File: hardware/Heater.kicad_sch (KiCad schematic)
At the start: 16 parts

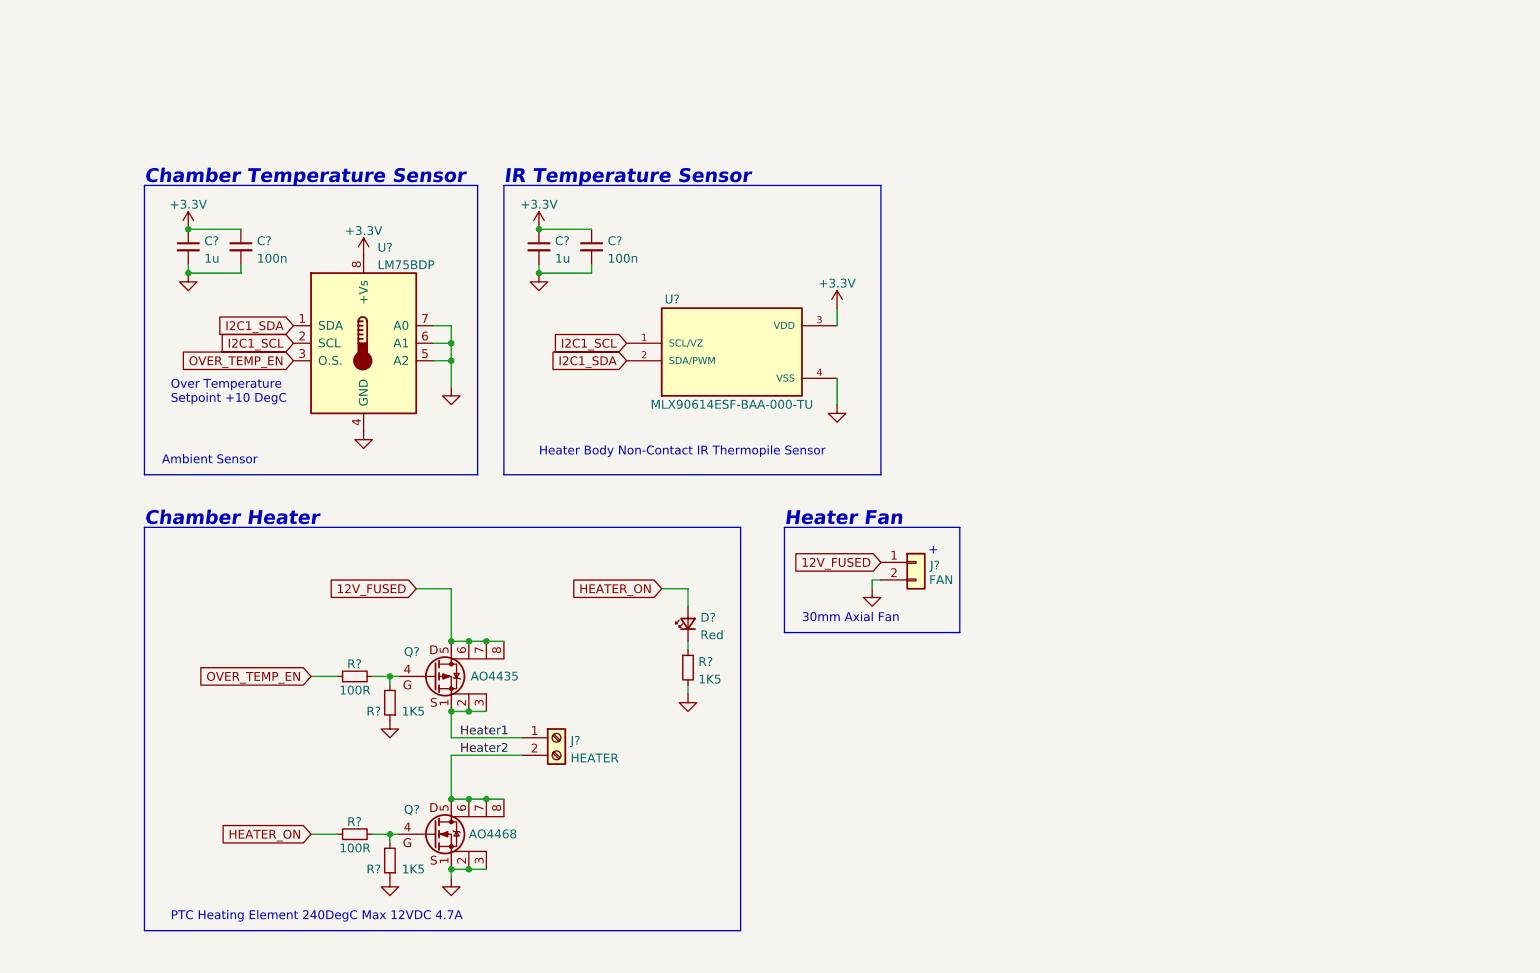
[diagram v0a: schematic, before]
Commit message: schematics finished, footprints assigned. Still need to fix foorptints for MOSFETS
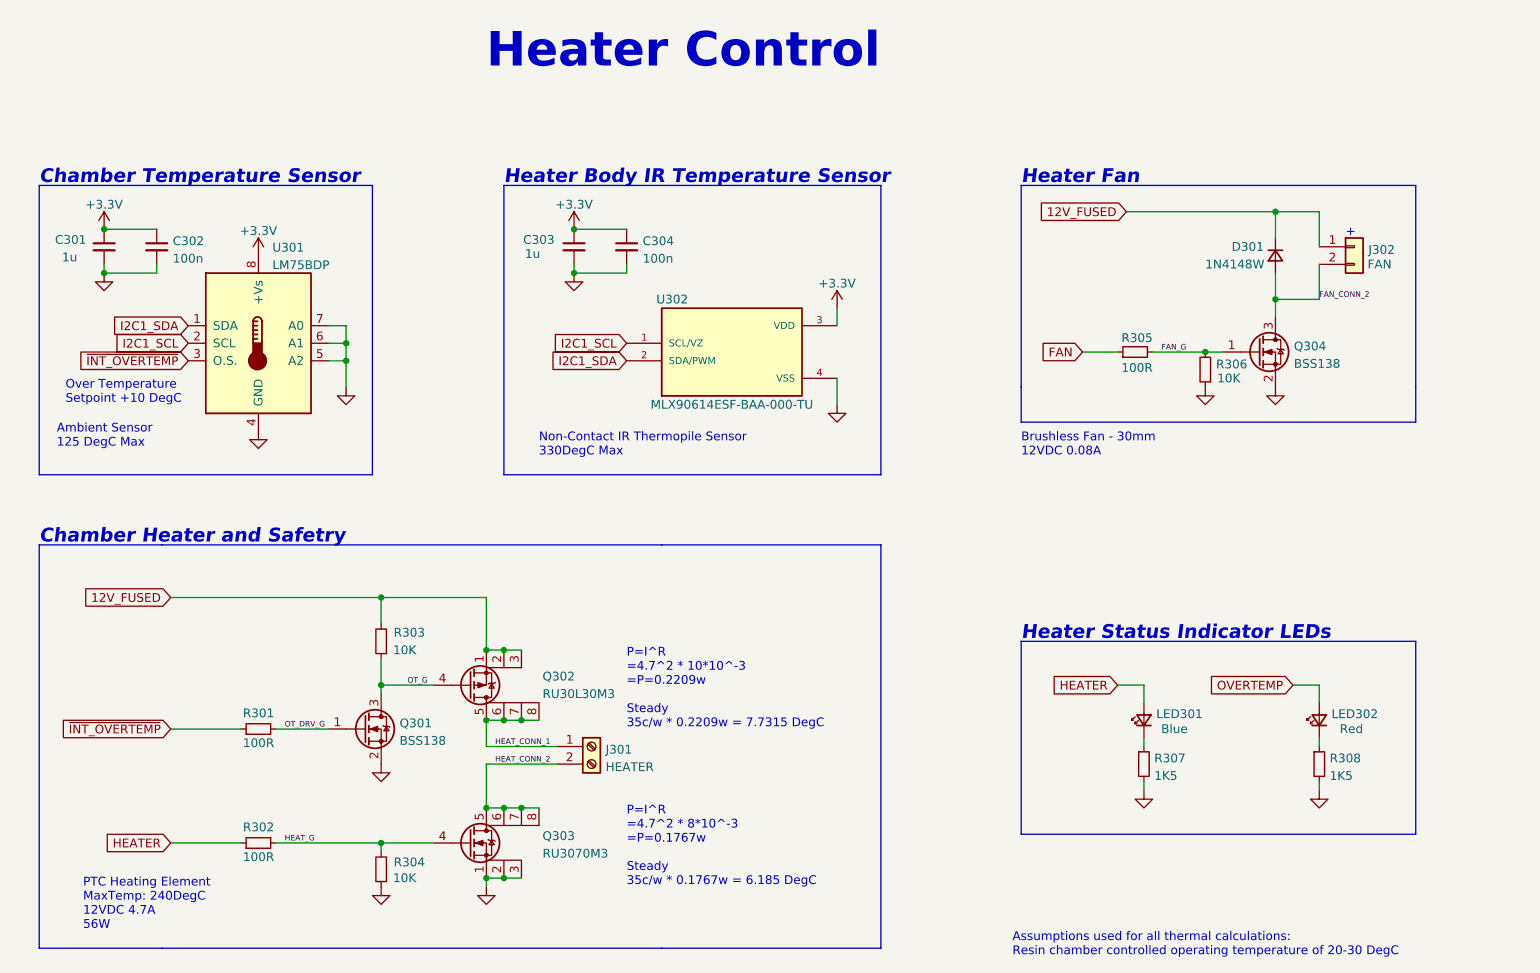
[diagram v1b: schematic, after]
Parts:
- removed D?: Red, symbol Device:LED_Small
- removed R?: 1K5, Resistor_SMD:R_0402_1005Metric, symbol Device:R_Small
- added D301: 1N4148W, Diode_SMD:D_SOD-123, symbol Device:D_Small
- added LED301: Blue, LED_SMD:LED_0603_1608Metric, symbol STR-LED:Blue
- added LED302: Red, LED_SMD:LED_0603_1608Metric, symbol STR-LED:Red
- added Q301, Q304: BSS138, Package_TO_SOT_SMD:SOT-23, symbol STR-MOSFETS:BSS138
- added R305: 100R, Resistor_SMD:R_0402_1005Metric, symbol Device:R_Small
- added R306: 10K, Resistor_SMD:R_0402_1005Metric, symbol Device:R_Small
- added R307, R308: 1K5, Resistor_SMD:R_0402_1005Metric, symbol Device:R_Small
- J301: renamed from J?; footprint (none) -> TerminalBlock_Phoenix:TerminalBlock_Phoenix_PT-1,5-2-3.5-H_1x02_P3.50mm_Horizontal
- J302: renamed from J?; footprint (none) -> Connector_JST:JST_EH_B2B-EH-A_1x02_P2.50mm_Vertical
- Q302: renamed from Q?; value AO4435 -> RU30L30M3; footprint Package_SO:SOIC-8-1EP_3.9x4.9mm_P1.27mm_EP2.29x3mm -> Package_DFN_QFN:DFN-8-1EP_3x3mm_P0.65mm_EP1.7x2.05mm; symbol STR-MOSFETS:AO4435 -> STR-MOSFETS:RU30L30M3; LCSC (none) -> C2895257; MANUFACTURER (none) -> Shenzhen ruichips Semicon; MPN (none) -> RU30L30M3
- Q303: renamed from Q?; value AO4468 -> RU3070M3; footprint Package_SO:SOIC-8-1EP_3.9x4.9mm_P1.27mm_EP2.29x3mm -> STR-DFN:DFN-8-1EP_3x3mm_P0.65mm_EP1.7x2.05mm; symbol STR-MOSFETS:AO4468 -> STR-MOSFETS:RU30L70M3
- R303, R304: renamed from R?; value 1K5 -> 10K
- U302: renamed from U?; footprint TO254P942H425-4 -> STR-Sensors:TO254P942H425-4
- gave numbers to parts that had none: 7
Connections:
- net 12V_FUSED: now also Q302.1 (S), Q302.2 (S), Q302.3 (S), R303.2, D301.1 (K); no longer Q302.5 (D), Q302.6 (D), Q302.7 (D), Q302.8 (D)
- net GND: now also Q301.2 (S), Q304.2 (S), R306.1, R307.2, R308.2; no longer J302.2 (Pin_2), R303.1
- net HEAT_G: now reaches Q303.4 (G), R302.2, R304.2
- net HEATER_ON renamed HEATER
- net HEATER: now also LED301.2 (A)
- removed net Heater1: J301.1 (Pin_1), Q302.1 (S), Q302.2 (S), Q302.3 (S)
- net Heater2 renamed HEAT_CONN_2
- net OVER_TEMP_EN renamed ~{INT_OVERTEMP}
- new net: LED301.1 (K), R307.1
- new net: LED302.1 (K), R308.1
- new net FAN: R305.1
- new net FAN_CONN_2: D301.2 (A), J302.2 (Pin_2), Q304.3 (D)
- new net FAN_G: Q304.1 (G), R305.2, R306.2
- new net HEAT_CONN_1: J301.1 (Pin_1), Q302.5 (D), Q302.6 (D), Q302.7 (D), Q302.8 (D)
- new net OT_DRV_G: Q301.1 (G), R301.2
- new net OT_G: Q301.3 (D), Q302.4 (G), R303.1
- new net OVERTEMP: LED302.2 (A)
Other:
- note added: "Ambient Sensor 125 DegC Max"
- note added: "Assumptions used for all thermal calculations: Resin chamber controlled operating temperature of 20-30 DegC"
- note added: "Brushless Fan - 30mm 12VDC 0.08A"
- note added: "Chamber Heater and Safetry"
- note added: "Heater Body IR Temperature Sensor"
- note added: "Heater Control"
- note added: "Heater Status Indicator LEDs"
- note added: "Non-Contact IR Thermopile Sensor 330DegC Max"
- note added: "P=I^R =4.7^2 * 10*10^-3 =P=0.2209w Steady 35c/w * 0.2209w = 7.7315 DegC"
- note added: "P=I^R =4.7^2 * 8*10^-3 =P=0.1767w Steady 35c/w * 0.1767w = 6.185 DegC"
- note added: "PTC Heating Element MaxTemp: 240DegC 12VDC 4.7A 56W"
- note removed: "30mm Axial Fan"
- note removed: "Ambient Sensor"
- note removed: "Chamber Heater"
- note removed: "Heater Body Non-Contact IR Thermopile Sensor"
- note removed: "IR Temperature Sensor"
- note removed: "PTC Heating Element 240DegC Max 12VDC 4.7A"
- title: (none) -> SLA Chamber Hearter for Resin Printers
- moved on the sheet: C301, C302, C303, C304, J301, J302, R301, R302, R303, R304, U301

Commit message: footprint update for MOSFETS to PDFN3333
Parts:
- Q302: footprint Package_DFN_QFN:DFN-8-1EP_3x3mm_P0.65mm_EP1.7x2.05mm -> STR-DFN:PDFN3333
- Q303: footprint STR-DFN:DFN-8-1EP_3x3mm_P0.65mm_EP1.7x2.05mm -> STR-DFN:PDFN3333
- U301: footprint Package_SO:MSOP-8-1EP_3x3mm_P0.65mm_EP1.68x1.88mm -> Package_SO:SOIC-8_3.9x4.9mm_P1.27mm
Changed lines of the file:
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@@
       (effects (font (size 1.27 1.27)) (justify left))
     )
-    (property "Footprint" "STR-DFN:DFN-8-1EP_3x3mm_P0.65mm_EP1.7x2.05mm" (id 2) (at 125.73 146.685 0)
+    (property "Footprint" "STR-DFN:PDFN3333" (id 2) (at 125.73 146.685 0)
       (effects (font (size 1.27 1.27) italic) (justify left) hide)
     )
@@
       (effects (font (size 1.27 1.27)) (justify left))
     )
-    (property "Footprint" "Package_SO:MSOP-8-1EP_3x3mm_P0.65mm_EP1.68x1.88mm" (id 2) (at 90.17 72.39 0)
+    (property "Footprint" "Package_SO:SOIC-8_3.9x4.9mm_P1.27mm" (id 2) (at 90.17 72.39 0)
       (effects (font (size 1.27 1.27)) hide)
     )
@@
       (effects (font (size 1.27 1.27)) (justify left))
     )
-    (property "Footprint" "Package_DFN_QFN:DFN-8-1EP_3x3mm_P0.65mm_EP1.7x2.05mm" (id 2) (at 125.73 120.015 0)
+    (property "Footprint" "STR-DFN:PDFN3333" (id 2) (at 125.73 120.015 0)
       (effects (font (size 1.27 1.27) italic) (justify left) hide)
     )

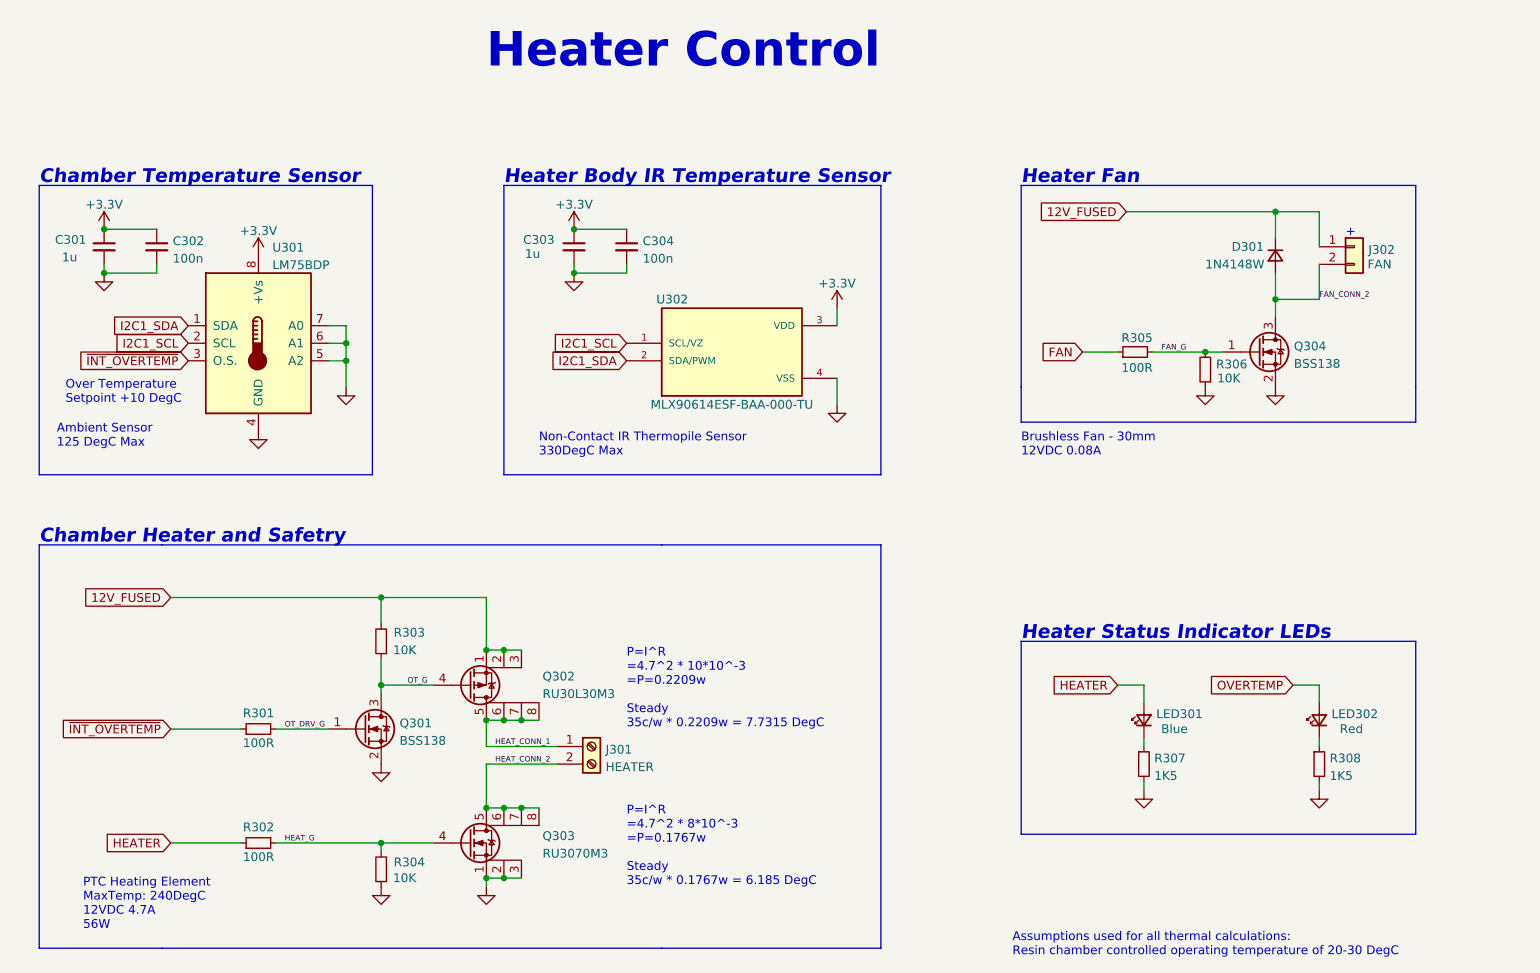
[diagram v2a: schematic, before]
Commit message: routing and foot print changes
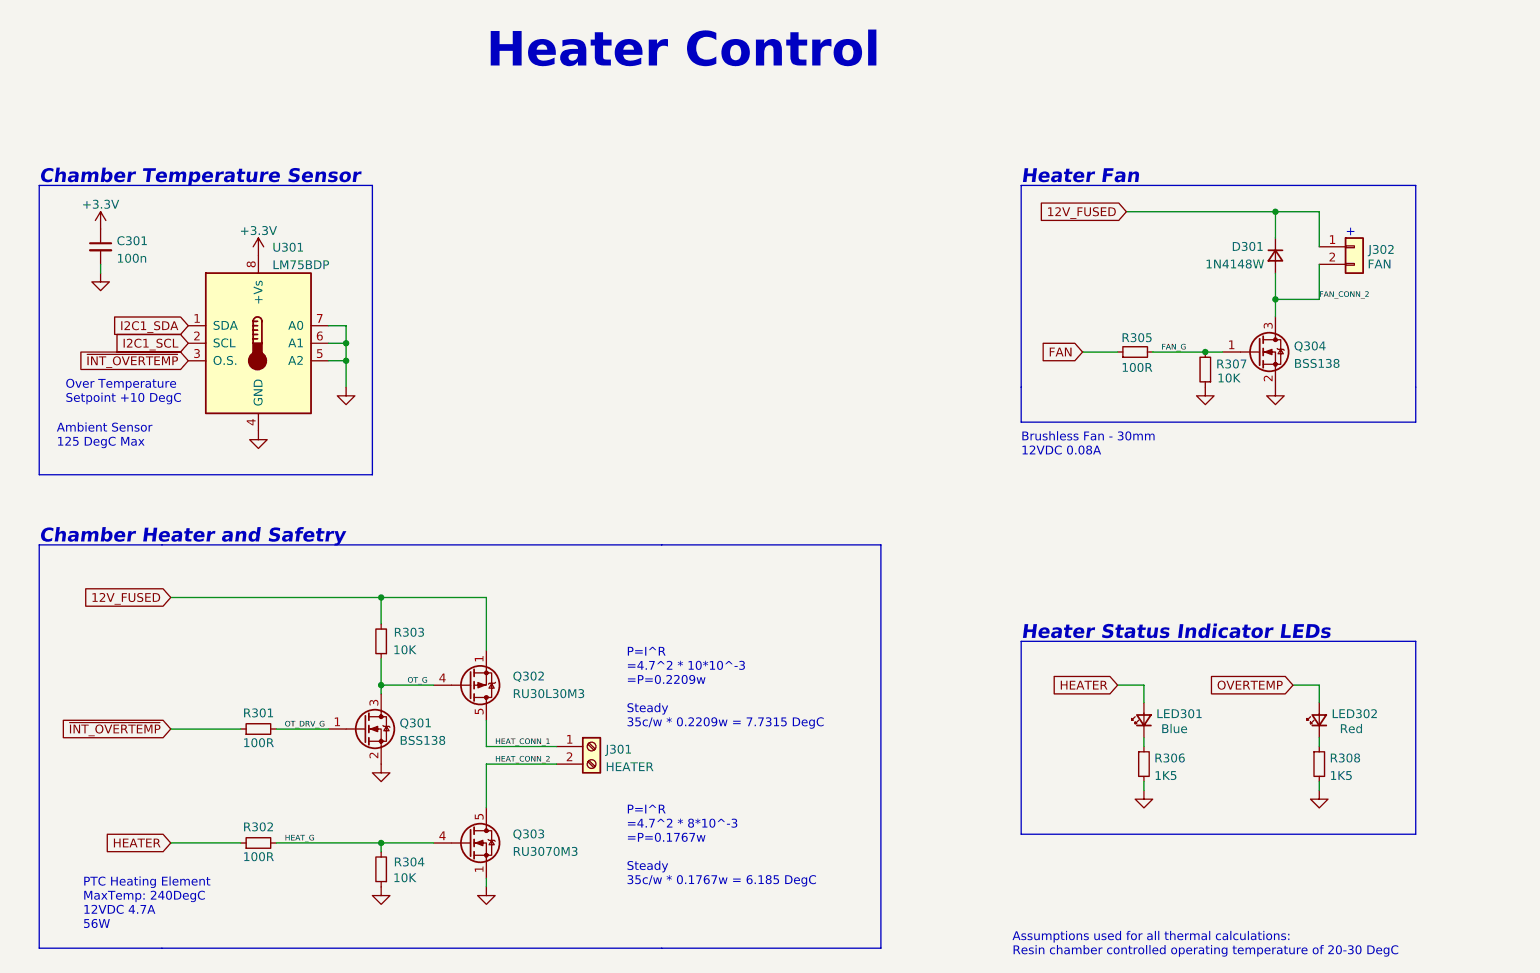
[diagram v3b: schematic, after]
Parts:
- removed C301, C303: 1u, Capacitor_SMD:C_0402_1005Metric, symbol Device:C_Small
- removed C304: 100n, Capacitor_SMD:C_0402_1005Metric, symbol Device:C_Small
- removed U302: MLX90614ESF-BAA-000-TU, STR-Sensors:TO254P942H425-4, symbol STR-Sensors:MLX90614ESF-BAA-000-TU
- J302: footprint Connector_JST:JST_EH_B2B-EH-A_1x02_P2.50mm_Vertical -> Connector_JST:JST_PH_B2B-PH-K_1x02_P2.00mm_Vertical
- Q302: footprint STR-DFN:PDFN3333 -> STR-DFN:DFN-8_L3.0-W3.0-P0.65-BL; symbol STR-MOSFETS:RU30L30M3 -> STR-MOSFETS:RU3030M3
- Q303: footprint STR-DFN:PDFN3333 -> STR-DFN:DFN-8_L3.0-W3.0-P0.65-BL; symbol STR-MOSFETS:RU30L70M3 -> STR-MOSFETS:RU3070M3
- renumbered C302 to C301, R307 to R306, R306 to R307
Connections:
- net HEAT_CONN_1: now also Q302.9 (D)
- net HEAT_CONN_2: now also Q303.9 (D)
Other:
- note removed: "Heater Body IR Temperature Sensor"
- note removed: "Non-Contact IR Thermopile Sensor 330DegC Max"
- moved on the sheet: C301
